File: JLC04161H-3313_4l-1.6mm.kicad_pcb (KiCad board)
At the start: 6 copper layers, 24 x 24 mm, 0 parts

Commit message: update stack
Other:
- copper layers 6 -> 4
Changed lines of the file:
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@@
 	(generator_version "8.0")
 	(general
-		(thickness 1.5484)
+		(thickness 1.5742)
 		(legacy_teardrops no)
 	)
@@
 		(date "SET!!!")
 		(rev "VERV")
-		(company "ELT")
+		(company "SET!!!")
 		(comment 2 "SET!!!")
 		(comment 3 "SET!!!")
 	)
 	(layers
-		(0 "F.Cu" mixed)
+		(0 "F.Cu" signal)
 		(1 "In1.Cu" power)
-		(2 "In2.Cu" signal)
-		(3 "In3.Cu" power)
-		(4 "In4.Cu" power)
+		(2 "In2.Cu" power)
 		(31 "B.Cu" signal)
 		(32 "B.Adhes" user "B.Adhesive")
@@
 			(layer "F.Mask"
 				(type "Top Solder Mask")
-				(color "Green")
 				(thickness 0.005)
 			)
@@
 			(layer "dielectric 1"
 				(type "prepreg")
-				(thickness 0.0994)
+				(thickness 0.0994 locked)
 				(material "3313")
-				(epsilon_r 4.5)
-				(loss_tangent 0.02)
+				(epsilon_r 4.1)
+				(loss_tangent 0.002)
 			)
 			(layer "In1.Cu"
@@
 			(layer "dielectric 2"
 				(type "core")
-				(thickness 0.55)
+				(color "FR4 natural")
+				(thickness 1.265 locked)
 				(material "FR4")
-				(epsilon_r 4.5)
+				(epsilon_r 4.6)
 				(loss_tangent 0.02)
 			)
@@
 			(layer "dielectric 3"
 				(type "prepreg")
-				(thickness 0.1088)
-				(material "2216")
-				(epsilon_r 4.5)
-				(loss_tangent 0.02)
-			)
-			(layer "In3.Cu"
-				(type "copper")
-				(thickness 0.0152)
-			)
-			(layer "dielectric 4"
-				(type "core")
-				(thickness 0.55)
-				(material "FR4")
-				(epsilon_r 4.5)
-				(loss_tangent 0.02)
-			)
-			(layer "In4.Cu"
-				(type "copper")
-				(thickness 0.0152)
-			)
-			(layer "dielectric 5"
-				(type "prepreg")
-				(thickness 0.0994)
+				(thickness 0.0994 locked)
 				(material "3313")
-				(epsilon_r 4.5)
-				(loss_tangent 0.02)
+				(epsilon_r 4.1)
+				(loss_tangent 0.002)
 			)
 			(layer "B.Cu"
@@
 			(layer "B.Mask"
 				(type "Bottom Solder Mask")
-				(color "Green")
 				(thickness 0.005)
 			)
@@
 				(type "Bottom Silk Screen")
 			)
-			(copper_finish "Immersion gold")
-			(dielectric_constraints no)
+			(copper_finish "HAL SnPb")
+			(dielectric_constraints yes)
 		)
 		(pad_to_mask_clearance 0)
@@
 		(layer "Dwgs.User")
 	)
+	(gr_arc
+		(start 34.000001 54.000001)
+		(mid 31.171573 52.828428)
+		(end 30 50)
+		(stroke
+			(width 0.1)
+			(type default)
+		)
+		(layer "Edge.Cuts")
+	)
+	(gr_arc
+		(start 50 30)
+		(mid 52.828428 31.171573)
+		(end 54.000001 34.000001)
+		(stroke
+			(width 0.1)
+			(type default)
+		)
+		(layer "Edge.Cuts")
+	)
 	(gr_line
 		(start 34 30)
 		(end 50 30)
+		(stroke
+			(width 0.1)
+			(type default)
+		)
+		(layer "Edge.Cuts")
+	)
+	(gr_arc
+		(start 54 50)
+		(mid 52.828427 52.828428)
+		(end 49.999999 54.000001)
+		(stroke
+			(width 0.1)
+			(type default)
+		)
+		(layer "Edge.Cuts")
+	)
+	(gr_line
+		(start 54 49.999999)
+		(end 54 34)
+		(stroke
+			(width 0.1)
+			(type default)
+		)
+		(layer "Edge.Cuts")
+	)
+	(gr_line
+		(start 49.999999 54.000001)
+		(end 33.999999 54.000001)
 		(stroke
 			(width 0.1)
@@
 		(layer "Edge.Cuts")
 	)
-	(gr_arc
-		(start 50 30)
-		(mid 52.828428 31.171573)
-		(end 54.000001 34.000001)
-		(stroke
-			(width 0.1)
-			(type default)
-		)
-		(layer "Edge.Cuts")
-	)
-	(gr_arc
-		(start 54 50)
-		(mid 52.828427 52.828428)
-		(end 49.999999 54.000001)
-		(stroke
-			(width 0.1)
-			(type default)
-		)
-		(layer "Edge.Cuts")
-	)
 	(gr_line
 		(start 29.999999 34.000001)
@@
 		(stroke
 			(width 0.1)
-			(type default)
-		)
-		(layer "Edge.Cuts")
-	)
-	(gr_line
-		(start 49.999999 54.000001)
-		(end 34 54.000001)
-		(stroke
-			(width 0.1)
-			(type default)
-		)
-		(layer "Edge.Cuts")
-	)
-	(gr_arc
-		(start 34 54.000001)
-		(mid 31.171572 52.828428)
-		(end 29.999999 50)
-		(stroke
-			(width 0.1)
-			(type default)
-		)
-		(layer "Edge.Cuts")
-	)
-	(gr_line
-		(start 54 49.999999)
-		(end 54 34)
-		(stroke
-			(width 0.1)

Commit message: add default zone
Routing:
- added copper zone on F.Cu, net (none)
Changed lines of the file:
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@@
 		(layer "Edge.Cuts")
 	)
+	(zone
+		(net 0)
+		(net_name "")
+		(layer "F.Cu")
+		(hatch edge 0.5)
+		(connect_pads
+			(clearance 0.127)
+		)
+		(min_thickness 0.127)
+		(filled_areas_thickness no)
+		(fill
+			(thermal_gap 0.127)
+			(thermal_bridge_width 0.5)
+			(smoothing fillet)
+			(radius 1)
+			(island_removal_mode 1)
+			(island_area_min 10)
+		)
+		(polygon
+			(pts
+				(xy 29 29) (xy 55 29) (xy 55 55) (xy 29 55)
+			)
+		)
+	)
 )

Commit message: update
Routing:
- added copper zone on B.Cu, net (none)
- added copper zone on In1.Cu, net (none)
- added copper zone on In2.Cu, net (none)
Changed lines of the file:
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@@
 		(net 0)
 		(net_name "")
-		(layer "F.Cu")
+		(layers "F&B.Cu")
 		(hatch edge 0.5)
 		(connect_pads
@@
 			)
 		)
+	)
+	(zone
+		(net 0)
+		(net_name "")
+		(layers "In1.Cu" "In2.Cu")
+		(hatch edge 0.5)
+		(priority 1)
+		(connect_pads
+			(clearance 0.2)
+		)
+		(min_thickness 0.2)
+		(filled_areas_thickness no)
+		(fill
+			(thermal_gap 0.2)
+			(thermal_bridge_width 0.5)
+			(smoothing fillet)
+			(radius 1)
+			(island_removal_mode 1)
+			(island_area_min 10)
+		)
+		(polygon
+			(pts
+				(xy 28 28) (xy 56 28) (xy 56 56) (xy 28 56)
+			)
+		)

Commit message: update silk
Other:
- board text added: "JLCJLCJLCJLC"
- board text added: "TES"
- board text added: "VERV"
- board text added: "test test test"
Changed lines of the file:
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@@
 	(net 0 "")
+	(gr_line
+		(start 49.999999 38.124999)
+		(end 47.750001 38.124998)
+		(stroke
+			(width 0.1)
+			(type default)
+		)
+		(layer "F.SilkS")
+	)
+	(gr_rect
+		(start 38 40)
+		(end 43 45)
+		(stroke
+			(width 0.1)
+			(type solid)
+		)
+		(fill solid)
+		(layer "F.SilkS")
+	)
+	(gr_line
+		(start 47.75 35.874999)
+		(end 47.750001 38.124998)
+		(stroke
+			(width 0.1)
+			(type default)
+		)
+		(layer "F.SilkS")
+	)
+	(gr_line
+		(start 50 35.875)
+		(end 47.75 35.874999)
+		(stroke
+			(width 0.1)
+			(type default)
+		)
+		(layer "F.SilkS")
+	)
+	(gr_line
+		(start 49.999999 38.124999)
+		(end 50 35.875)
+		(stroke
+			(width 0.1)
+			(type default)
+		)
+		(layer "F.SilkS")
+	)
 	(gr_line
 		(start 30 31)
@@
 		)
 		(layer "Edge.Cuts")
+	)
+	(gr_text "VERV"
+		(at 47 36.624999 0)
+		(layer "F.SilkS")
+		(effects
+			(font
+				(size 0.8 0.8)
+				(thickness 0.15)
+				(bold yes)
+				(italic yes)
+			)
+			(justify right)
+		)
+	)
+	(gr_text "TES"
+		(at 38.75 36.5 0)
+		(layer "F.SilkS")
+		(effects
+			(font
+				(size 1 1)
+				(thickness 0.2)
+				(bold yes)
+				(italic yes)
+			)
+			(justify left)
+		)
+	)
+	(gr_text "JLCJLCJLCJLC"
+		(at 43 46 0)
+		(layer "F.SilkS")
+		(effects
+			(font
+				(size 0.8 0.8)
+				(thickness 0.15)
+			)
+		)
+	)
+	(gr_text "test test test"
+		(at 38.75 37.749999 0)
+		(layer "F.SilkS")
+		(effects
+			(font
+				(size 0.8 0.8)
+				(thickness 0.15)
+				(bold yes)
+			)
+			(justify left)
+		)
+	)
+	(dimension
+		(type aligned)
+		(layer "Dwgs.User")
+		(pts
+			(xy 30 50) (xy 54 50)
+		)
+		(height 7.999999)
+		(gr_text "24,0000 mm"
+			(at 42 56.849999 0)
+			(layer "Dwgs.User")
+			(effects
+				(font
+					(size 1 1)
+					(thickness 0.15)
+				)
+			)
+		)
+		(format
+			(prefix "")
+			(suffix "")
+			(units 3)
+			(units_format 1)
+			(precision 4)
+		)
+		(style
+			(thickness 0.1)
+			(arrow_length 1.27)
+			(text_position_mode 0)
+			(extension_height 0.58642)
+			(extension_offset 0.5) keep_text_aligned)
+	)
+	(dimension
+		(type aligned)
+		(layer "Dwgs.User")
+		(pts
+			(xy 50 54.000001) (xy 50 30)
+		)
+		(height 7.999999)
+		(gr_text "24,0000 mm"
+			(at 56.849999 42 90)
+			(layer "Dwgs.User")
+			(effects
+				(font
+					(size 1 1)
+					(thickness 0.15)
+				)
+			)
+		)
+		(format
+			(prefix "")
+			(suffix "")
+			(units 3)
+			(units_format 1)
+			(precision 4)
+		)
+		(style
+			(thickness 0.1)
+			(arrow_length 1.27)
+			(text_position_mode 0)
+			(extension_height 0.58642)
+			(extension_offset 0.5) keep_text_aligned)
 	)
 	(zone
@@
 		)
 	)
+	(group ""
+		(members "0240af20-a752-4780-a926-65fbc60f5358" "237b0341-8d15-497a-8d30-9d6c12a84ab4"
+			"2ed620ba-2978-4037-95af-29875a943be1" "9a91648a-59d1-4ab8-abd2-b40810229923"
+		)
+	)
+	(group ""
+		(members "729a2c77-b021-4f63-90b1-0bdd52d23476" "aa77a243-843f-457c-b03d-39b7605a39c0"
+			"f60b4e85-edb7-4ce6-bf66-f1e0ff2ec87d"
+		)
+	)
+	(group ""
+		(members "201dab69-6c33-4b40-8d06-5afe88b88437")
+	)
 )

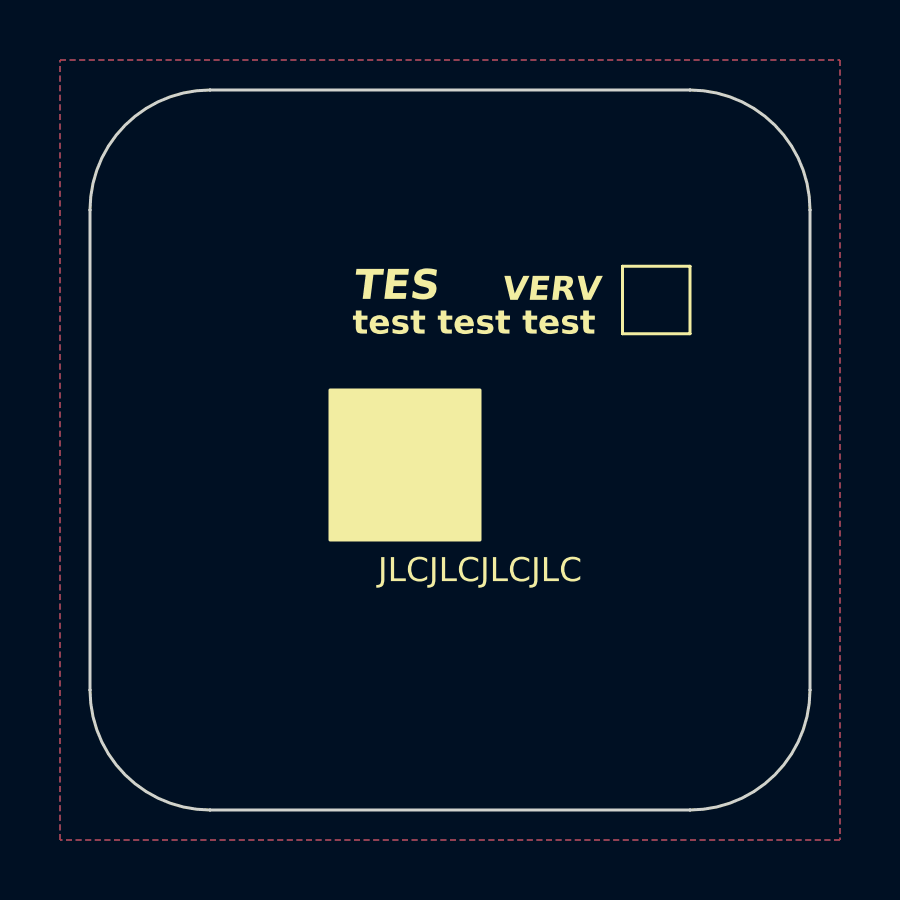
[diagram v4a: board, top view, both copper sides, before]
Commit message: Update to kicad9
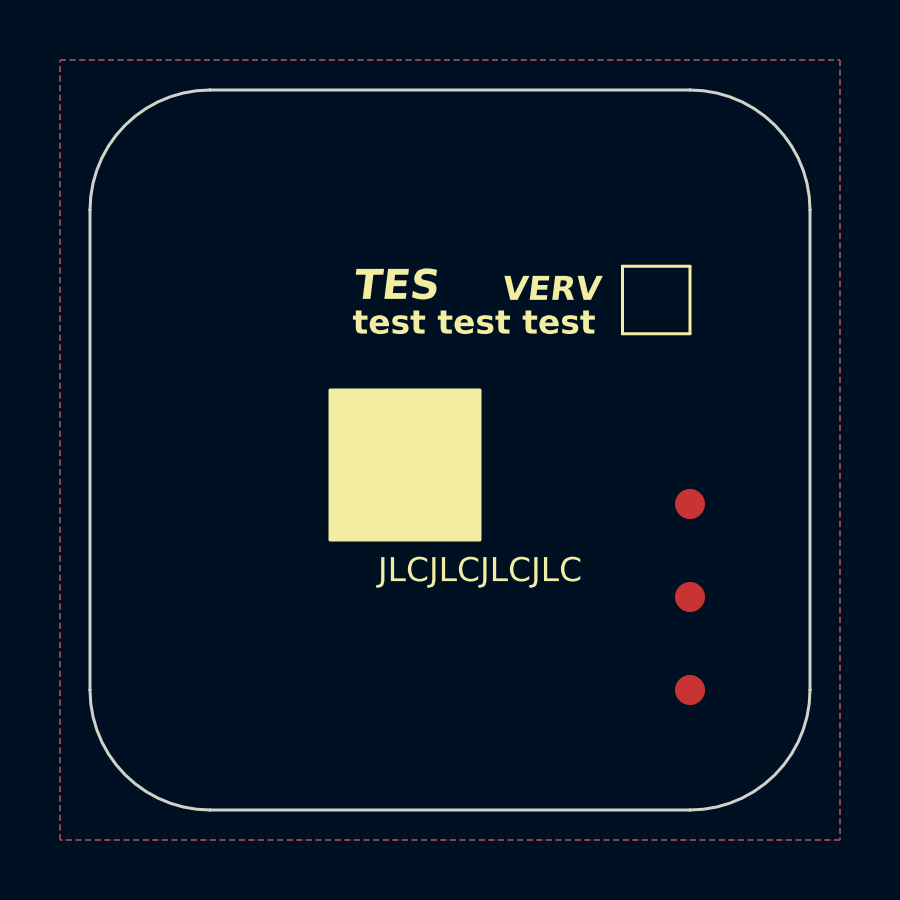
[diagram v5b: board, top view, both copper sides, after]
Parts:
- added FID1: Fiducial, MAS_Package_std:Fiducial_1mm_Mask2mm, F.Cu at (50.0, 43.8)
- added FID2: Fiducial, MAS_Package_std:Fiducial_1mm_Mask2mm, F.Cu at (50.0, 46.9)
- added FID3: Fiducial, MAS_Package_std:Fiducial_1mm_Mask2mm, F.Cu at (50.0, 50.0)
